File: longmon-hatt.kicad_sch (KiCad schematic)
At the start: 4 parts

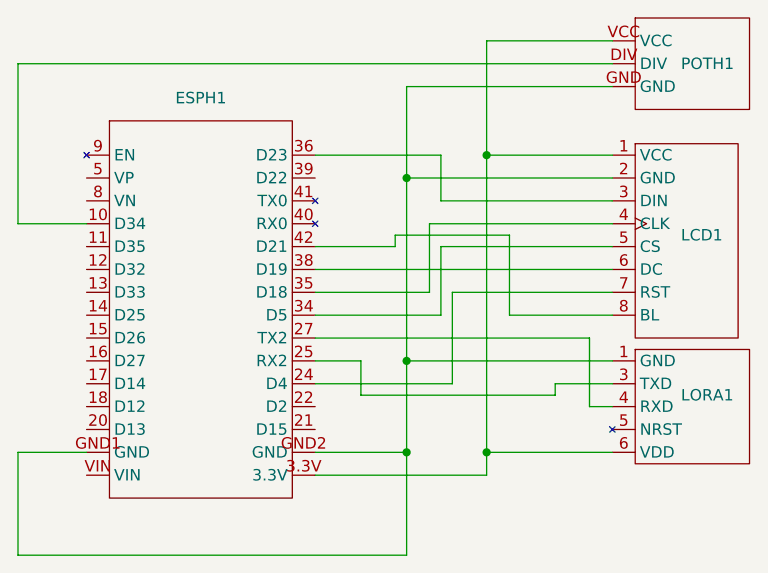
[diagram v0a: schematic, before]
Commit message: Fixed LCD pins not being connected bug
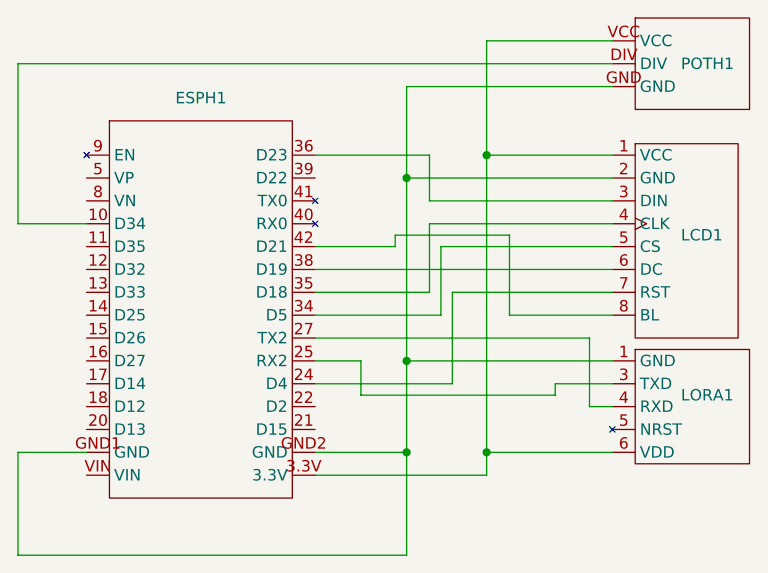
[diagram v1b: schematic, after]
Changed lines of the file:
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@@
 (kicad_sch (version 20230121) (generator eeschema)
   (paper "A4")
+  (junction (at 77.47 36.83) (diameter 0) (color 0 0 0 0)
+  )
   (junction (at 86.36 67.31) (diameter 0) (color 0 0 0 0)
   )
   (junction (at 77.47 57.15) (diameter 0) (color 0 0 0 0)
   )
-  (junction (at 86.36 34.29) (diameter 0) (color 0 0 0 0)
-  )
-  (junction (at 77.47 36.83) (diameter 0) (color 0 0 0 0)
-  )
   (junction (at 77.47 67.31) (diameter 0) (color 0 0 0 0)
   )
-  (wire (pts (xy 77.47 26.67) (xy 77.47 36.83))
-    (stroke (width 0) (type default))
+  (junction (at 86.36 34.29) (diameter 0) (color 0 0 0 0)
   )
   (wire (pts (xy 93.98 60.96) (xy 72.39 60.96))
@@
     (stroke (width 0) (type default))
   )
-  (wire (pts (xy 81.28 34.29) (xy 81.28 39.37))
+  (wire (pts (xy 77.47 36.83) (xy 77.47 57.15))
     (stroke (width 0) (type default))
   )
@@
     (stroke (width 0) (type default))
   )
+  (wire (pts (xy 80.01 39.37) (xy 80.01 34.29))
+    (stroke (width 0) (type default))
+  )
   (wire (pts (xy 77.47 67.31) (xy 67.31 67.31))
     (stroke (width 0) (type default))
   )
   (wire (pts (xy 34.29 41.91) (xy 41.91 41.91))
+    (stroke (width 0) (type default))
+  )
+  (wire (pts (xy 80.01 34.29) (xy 67.31 34.29))
     (stroke (width 0) (type default))
   )
@@
     (stroke (width 0) (type default))
   )
+  (wire (pts (xy 86.36 34.29) (xy 100.33 34.29))
+    (stroke (width 0) (type default))
+  )
   (wire (pts (xy 81.28 52.07) (xy 81.28 44.45))
     (stroke (width 0) (type default))
@@
   )
   (wire (pts (xy 77.47 67.31) (xy 77.47 78.74))
+    (stroke (width 0) (type default))
+  )
+  (wire (pts (xy 100.33 39.37) (xy 80.01 39.37))
     (stroke (width 0) (type default))
   )
@@
     (stroke (width 0) (type default))
   )
-  (wire (pts (xy 67.31 34.29) (xy 81.28 34.29))
+  (wire (pts (xy 34.29 78.74) (xy 77.47 78.74))
     (stroke (width 0) (type default))
   )
-  (wire (pts (xy 100.33 36.83) (xy 77.47 36.83))
-    (stroke (width 0) (type default))
-  )
-  (wire (pts (xy 86.36 34.29) (xy 100.33 34.29))
-    (stroke (width 0) (type default))
-  )
-  (wire (pts (xy 86.36 34.29) (xy 86.36 21.59))
-    (stroke (width 0) (type default))
-  )
-  (wire (pts (xy 34.29 78.74) (xy 77.47 78.74))
+  (wire (pts (xy 77.47 36.83) (xy 100.33 36.83))
     (stroke (width 0) (type default))
   )
@@
     (stroke (width 0) (type default))
   )
+  (wire (pts (xy 86.36 34.29) (xy 86.36 67.31))
+    (stroke (width 0) (type default))
+  )
   (wire (pts (xy 77.47 57.15) (xy 77.47 67.31))
     (stroke (width 0) (type default))
   )
-  (wire (pts (xy 86.36 34.29) (xy 86.36 67.31))
+  (wire (pts (xy 86.36 21.59) (xy 86.36 34.29))
     (stroke (width 0) (type default))
   )
@@
     (stroke (width 0) (type default))
   )
-  (wire (pts (xy 77.47 36.83) (xy 77.47 57.15))
+  (wire (pts (xy 77.47 26.67) (xy 77.47 36.83))
     (stroke (width 0) (type default))
   )
@@
     (stroke (width 0) (type default))
   )
-  (wire (pts (xy 81.28 39.37) (xy 100.33 39.37))
-    (stroke (width 0) (type default))
-  )

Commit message: Replace ESP32 with imported library
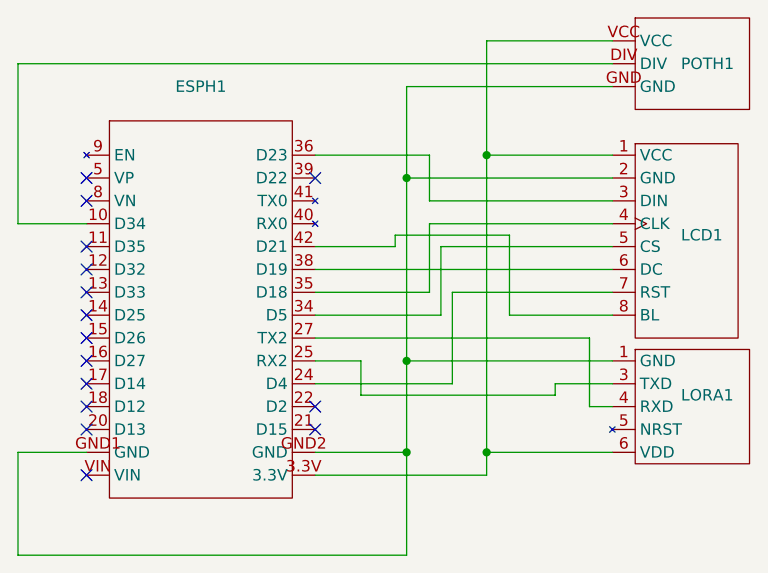
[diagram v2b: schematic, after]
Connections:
- no-connect marks 0 -> 15
